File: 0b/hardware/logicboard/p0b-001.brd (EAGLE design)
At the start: 70 x 41 mm, 30 parts, among them IC1 7404D, IC4 LTC485S, IC5 LTC485S, J0 DC5V, J7 DIN5, J9 DIN5, X7 NELTRON-7810-XPXC

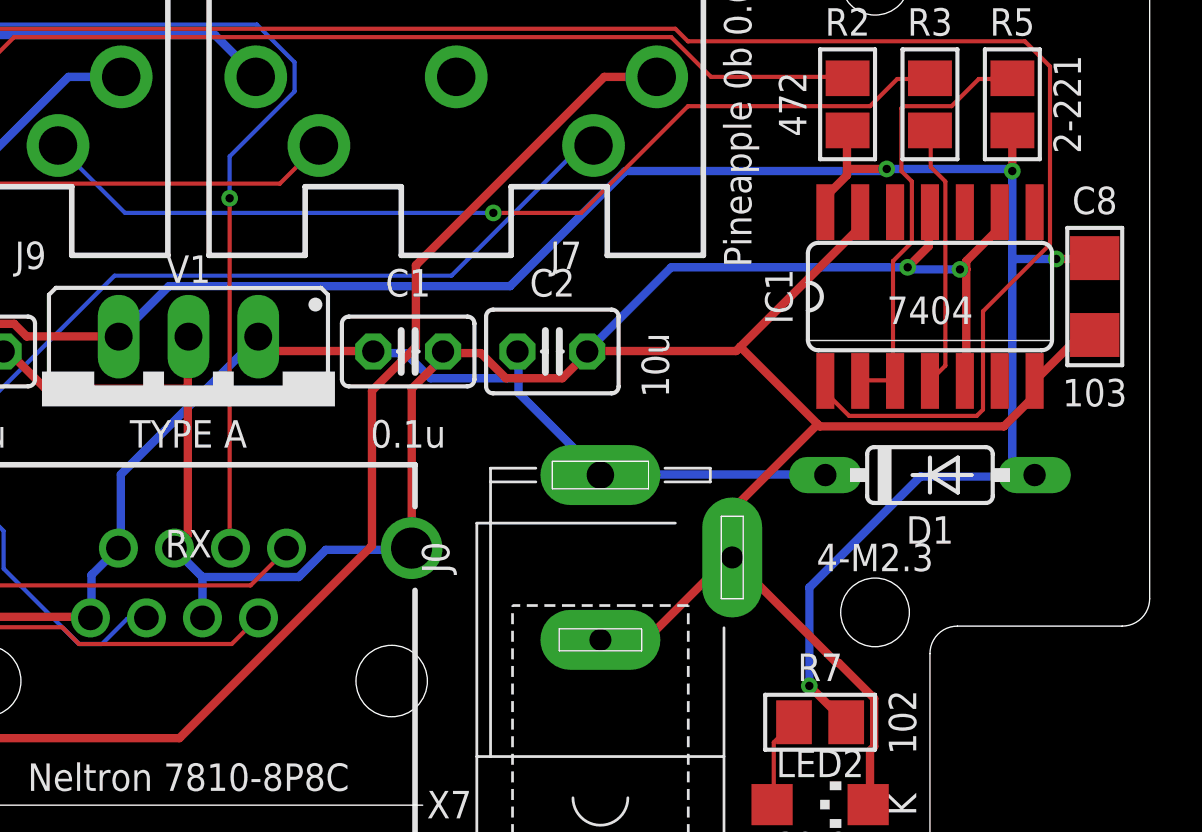
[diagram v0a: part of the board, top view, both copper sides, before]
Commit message: Added Direct-5V resistor pattern.
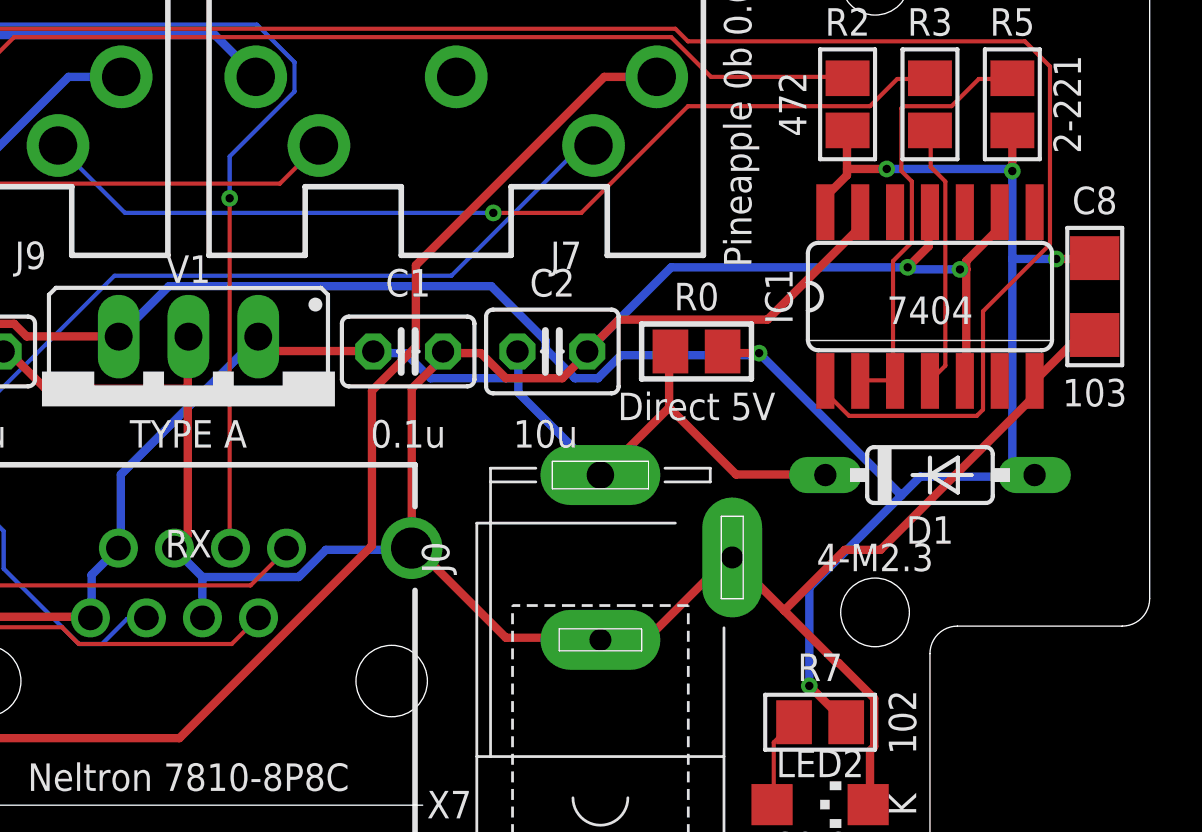
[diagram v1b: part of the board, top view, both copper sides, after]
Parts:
- added R0: Inf, rcl:M2012
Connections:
- net V+: now also R0.1
- net VCC: now also R0.2
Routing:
- net VCC: track 143.2 -> 147.4 mm, vias 8 -> 9
- net V+: track 52.6 -> 56.6 mm
- net GND: track 230.9 -> 233.0 mm
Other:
- board text added: "Direct 5V"

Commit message: Pinhead.
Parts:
- removed R0: Inf, rcl:M2012
- added JP1: (no value), pinhead:1X02
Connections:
- net V+: now also JP1.1; no longer R0.1
- net VCC: now also JP1.2; no longer R0.2
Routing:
- net VCC: track 147.4 -> 173.7 mm, vias 9 -> 7
- net GND: track 233.0 -> 215.7 mm
- net MIDIINGND: track 50.9 -> 55.4 mm
- net TX+: track 37.0 -> 40.1 mm
- net RX+: track 42.8 -> 44.7 mm, vias 1 -> 2
- net RX-: track 60.3 -> 59.3 mm, vias 3 -> 2
- net V+: track 56.6 -> 57.4 mm
- net RX: track 88.8 -> 89.5 mm
- net MIRTN: track 45.0 -> 44.6 mm, vias 3 -> 1
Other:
- board text added: "485"
- board text removed: "RX"

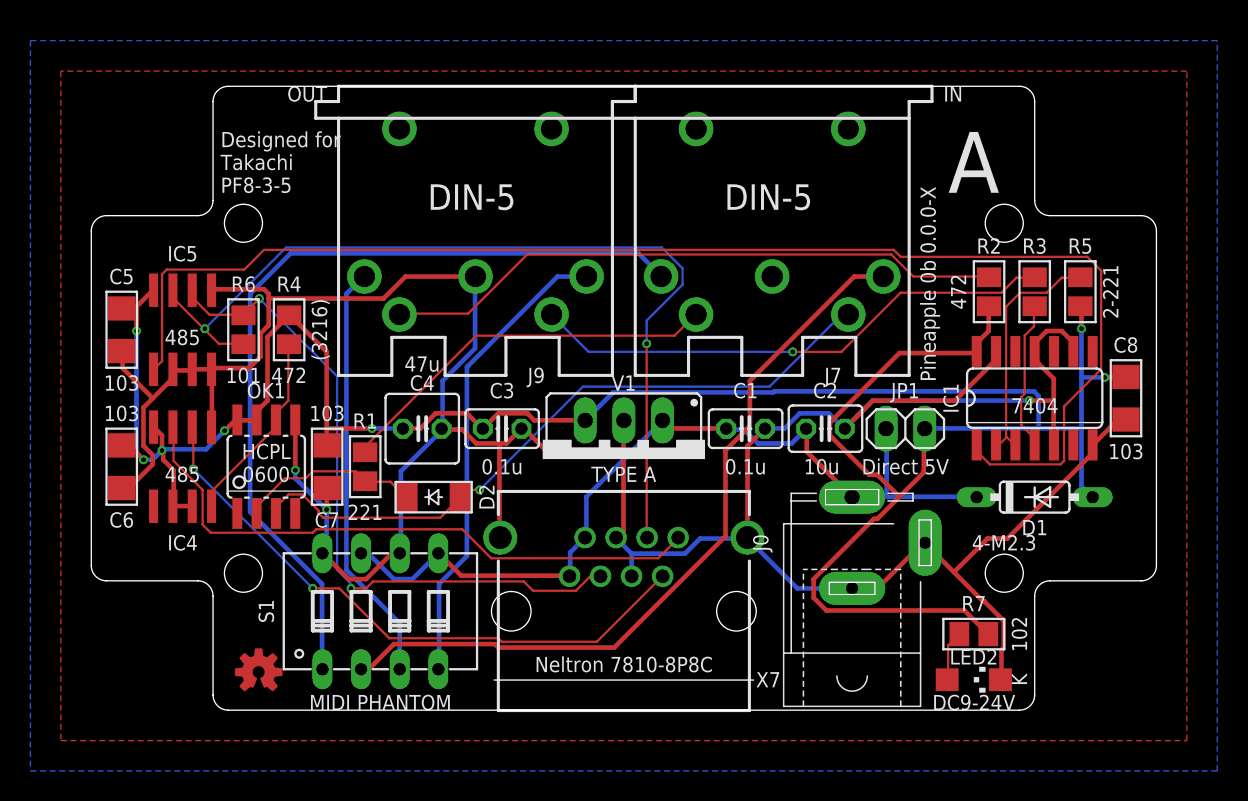
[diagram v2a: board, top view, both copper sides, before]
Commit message: Added PoE R.
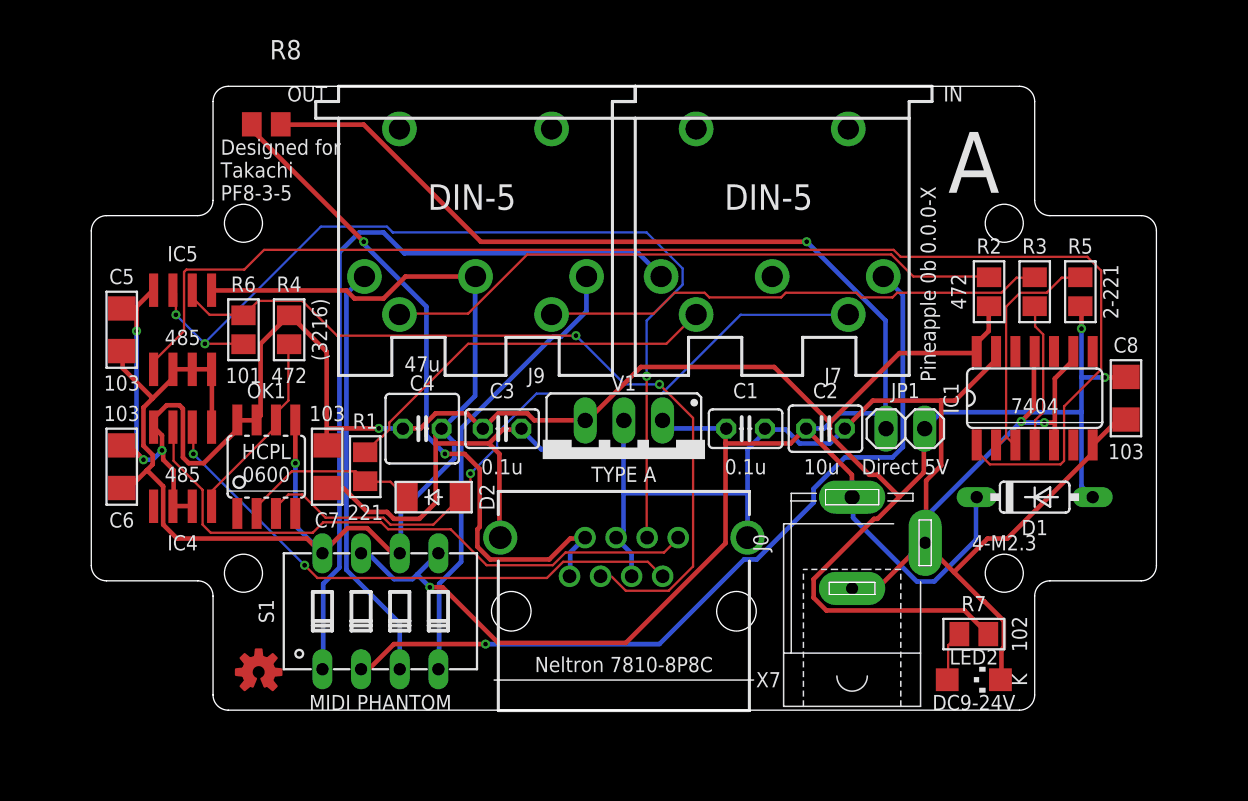
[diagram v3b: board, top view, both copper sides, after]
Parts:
- added R8: 0, rcl:M2012
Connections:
- new net POE: R8.1, X7.7, X7.8
- net V+: now also R8.2; no longer X7.7, X7.8
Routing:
- net V+: track 57.4 -> 128.7 mm, vias 0 -> 2
- net POE: track 0.00 -> 45.8 mm, vias 0 -> 2
- net GND: track 215.7 -> 236.4 mm
- net RX+: track 44.7 -> 54.4 mm
- net VCC: track 173.7 -> 166.0 mm, vias 7 -> 6
- net MIDIINGND: track 55.4 -> 50.8 mm
- net MIDIINV+: track 50.3 -> 54.0 mm, vias 0 -> 1
- net TX+: track 40.1 -> 36.9 mm
- net RX-: track 59.3 -> 61.4 mm, vias 2 -> 3
- net MORTN: track 34.8 -> 33.3 mm, vias 1 -> 0
- net MIRTN: track 44.6 -> 46.0 mm
- net MIDIOUTV+: track 31.0 -> 30.2 mm
- net RX: track 89.5 -> 88.8 mm
- net TX-: track 40.2 -> 40.9 mm
- removed copper zone on layer 1, net GND
- removed copper zone on layer 16, net GND

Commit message: Pinhead.
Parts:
- added JP2: (no value), pinhead:1X02
- R8: value 0 -> 20
- moved R8 6.96 mm to (14.0, 32.0), turned to 270 degrees
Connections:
- new net POERAW: JP2.1, R8.1
- net POE: now also JP2.2; no longer R8.1
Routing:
- net V+: track 128.7 -> 88.0 mm, vias 2 -> 1
- net RX: track 88.8 -> 68.9 mm, vias 0 -> 2
- net RX-: track 61.4 -> 41.7 mm, vias 3 -> 1
- net RX+: track 54.4 -> 38.6 mm, vias 2 -> 1
- net VCC: track 166.0 -> 178.9 mm, vias 6 -> 7
- net GND: track 236.4 -> 223.8 mm, vias 3 -> 1
- net POE: track 45.8 -> 55.2 mm, vias 2 -> 0
- net MIRTN: track 46.0 -> 54.7 mm, vias 1 -> 3
- net POERAW: track 0.00 -> 6.62 mm
- net MIDIINV+: track 54.0 -> 50.3 mm, vias 1 -> 0
- net TX+: track 36.9 -> 40.0 mm
- net TX-: track 40.9 -> 42.4 mm
- net MORTN: track 33.3 -> 34.5 mm, vias 0 -> 1
- net MIDIOUTV+: track 30.2 -> 31.0 mm
- net MIDIOUTGND: track 27.8 -> 27.0 mm
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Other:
- board text added: "(2012)"
- board text added: "20"
- board text added: "PoE"
- board text removed: "(3216)"
